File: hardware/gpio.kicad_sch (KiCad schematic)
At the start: 14 parts, among them U4 CCGM1A1

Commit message: Cleanup
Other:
- moved on the sheet: R115, R116, R117
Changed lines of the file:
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@@
 	(wire
 		(pts
-			(xy 234.95 35.56) (xy 234.95 38.1)
+			(xy 101.6 80.01) (xy 101.6 82.55)
 		)
 		(stroke
@@
 	(wire
 		(pts
-			(xy 229.87 35.56) (xy 229.87 38.1)
+			(xy 96.52 80.01) (xy 96.52 82.55)
 		)
 		(stroke
@@
 	(wire
 		(pts
-			(xy 234.95 25.4) (xy 234.95 30.48)
+			(xy 101.6 69.85) (xy 101.6 74.93)
 		)
 		(stroke
@@
 	(wire
 		(pts
-			(xy 224.79 30.48) (xy 224.79 25.4)
+			(xy 91.44 74.93) (xy 91.44 69.85)
 		)
 		(stroke
@@
 	(wire
 		(pts
-			(xy 224.79 35.56) (xy 224.79 38.1)
+			(xy 91.44 80.01) (xy 91.44 82.55)
 		)
 		(stroke
@@
 	(wire
 		(pts
-			(xy 229.87 25.4) (xy 229.87 30.48)
+			(xy 96.52 69.85) (xy 96.52 74.93)
 		)
 		(stroke
@@
 	(global_label "VDD_CLK"
 		(shape passive)
-		(at 229.87 25.4 90)
+		(at 96.52 69.85 90)
 		(fields_autoplaced yes)
 		(effects
@@
 		)
 		(property "Intersheetrefs" "${INTERSHEET_REFS}"
-			(at 229.87 15.3618 90)
+			(at 96.52 59.8118 90)
 			(effects
 				(font
@@
 	(symbol
 		(lib_id "Device:R_Small")
-		(at 229.87 33.02 180)
+		(at 96.52 77.47 180)
 		(unit 1)
 		(exclude_from_sim no)
@@
 		(dnp no)
 		(property "Reference" "R117"
-			(at 227.33 33.02 90)
+			(at 93.98 77.47 90)
 			(effects
 				(font
@@
 		)
 		(property "Value" "dnp"
-			(at 229.87 33.02 90)
+			(at 96.52 77.47 90)
 			(effects
 				(font
@@
 		)
 		(property "Footprint" "Resistor_SMD:R_0402_1005Metric"
-			(at 229.87 33.02 0)
+			(at 96.52 77.47 0)
 			(effects
 				(font
@@
 		)
 		(property "Datasheet" "~"
-			(at 229.87 33.02 0)
+			(at 96.52 77.47 0)
 			(effects
 				(font
@@
 		)
 		(property "Description" "Resistor, small symbol"
-			(at 229.87 33.02 0)
+			(at 96.52 77.47 0)
 			(effects
 				(font
@@
 	(symbol
 		(lib_id "power:VCC")
-		(at 229.87 38.1 180)
+		(at 96.52 82.55 180)
 		(unit 1)
 		(exclude_from_sim no)
@@
 		(dnp no)
 		(property "Reference" "#PWR0152"
-			(at 229.87 34.29 0)
+			(at 96.52 78.74 0)
 			(effects
 				(font
@@
 		)
 		(property "Value" "SDRAM_VCC"
-			(at 227.584 44.958 90)
+			(at 94.234 89.408 90)
 			(effects
 				(font
@@
 		)
 		(property "Footprint" ""
-			(at 229.87 38.1 0)
+			(at 96.52 82.55 0)
 			(effects
 				(font
@@
 		)
 		(property "Datasheet" ""
-			(at 229.87 38.1 0)
+			(at 96.52 82.55 0)
 			(effects
 				(font
@@
 		)
 		(property "Description" "Power symbol creates a global label with name \"VCC\""
-			(at 229.87 38.1 0)
+			(at 96.52 82.55 0)
 			(effects
 				(font
@@
 		(lib_name "+3V3_1")
 		(lib_id "power:+3V3")
-		(at 234.95 25.4 0)
+		(at 101.6 69.85 0)
 		(unit 1)
 		(exclude_from_sim no)
@@
 		(dnp no)
 		(property "Reference" "#PWR0135"
-			(at 234.95 29.21 0)
+			(at 101.6 73.66 0)
 			(effects
 				(font
@@
 		)
 		(property "Value" "+3V3"
-			(at 234.95 20.32 90)
+			(at 101.6 64.77 90)
 			(effects
 				(font
@@
 		)
 		(property "Footprint" ""
-			(at 234.95 25.4 0)
+			(at 101.6 69.85 0)
 			(effects
 				(font
@@
 		)
 		(property "Datasheet" ""
-			(at 234.95 25.4 0)
+			(at 101.6 69.85 0)
 			(effects
 				(font
@@
 		)
 		(property "Description" "Power symbol creates a global label with name \"+3V3\""
-			(at 234.95 25.4 0)
+			(at 101.6 69.85 0)
 			(effects
 				(font
@@
 	(symbol
 		(lib_id "Device:R_Small")
-		(at 234.95 33.02 180)
+		(at 101.6 77.47 180)
 		(unit 1)
 		(exclude_from_sim no)
@@
 		(dnp no)
 		(property "Reference" "R115"
-			(at 232.41 33.02 90)
+			(at 99.06 77.47 90)
 			(effects
 				(font
@@
 		)
 		(property "Value" "dnp"
-			(at 234.95 33.02 90)
+			(at 101.6 77.47 90)
 			(effects
 				(font
@@
 		)
 		(property "Footprint" "Resistor_SMD:R_0402_1005Metric"
-			(at 234.95 33.02 0)
+			(at 101.6 77.47 0)
 			(effects
 				(font
@@
 		)
 		(property "Datasheet" "~"
-			(at 234.95 33.02 0)
+			(at 101.6 77.47 0)
 			(effects
 				(font
@@
 		)
 		(property "Description" "Resistor, small symbol"
-			(at 234.95 33.02 0)
+			(at 101.6 77.47 0)
 			(effects
 				(font
@@
 	(symbol
 		(lib_id "power:+1V8")
-		(at 224.79 25.4 0)
+		(at 91.44 69.85 0)
 		(unit 1)
 		(exclude_from_sim no)
@@
 		(dnp no)
 		(property "Reference" "#PWR091"
-			(at 224.79 29.21 0)
+			(at 91.44 73.66 0)
 			(effects
 				(font
@@
 		)
 		(property "Value" "+1V8"
-			(at 224.79 20.32 90)
+			(at 91.44 64.77 90)
 			(effects
 				(font
@@
 		)
 		(property "Footprint" ""
-			(at 224.79 25.4 0)
+			(at 91.44 69.85 0)
 			(effects
 				(font
@@
 		)
 		(property "Datasheet" ""
-			(at 224.79 25.4 0)
+			(at 91.44 69.85 0)
 			(effects
 				(font
@@
 		)
 		(property "Description" "Power symbol creates a global label with name \"+1V8\""
-			(at 224.79 25.4 0)
+			(at 91.44 69.85 0)
 			(effects
 				(font
@@
 	(symbol
 		(lib_id "power:VCC")
-		(at 234.95 38.1 180)
+		(at 101.6 82.55 180)
 		(unit 1)
 		(exclude_from_sim no)
@@
 		(dnp no)
 		(property "Reference" "#PWR0151"
-			(at 234.95 34.29 0)
+			(at 101.6 78.74 0)
 			(effects
 				(font
@@
 		)
 		(property "Value" "SDRAM_VCC"
-			(at 232.664 44.958 90)
+			(at 99.314 89.408 90)
 			(effects
 				(font
@@
 		)
 		(property "Footprint" ""
-			(at 234.95 38.1 0)
+			(at 101.6 82.55 0)
 			(effects
 				(font
@@
 		)
 		(property "Datasheet" ""
-			(at 234.95 38.1 0)
+			(at 101.6 82.55 0)
 			(effects
 				(font
@@
 		)
 		(property "Description" "Power symbol creates a global label with name \"VCC\""
-			(at 234.95 38.1 0)
+			(at 101.6 82.55 0)
 			(effects
 				(font
@@
 	(symbol
 		(lib_id "power:VCC")
-		(at 224.79 38.1 180)
+		(at 91.44 82.55 180)
 		(unit 1)
 		(exclude_from_sim no)
@@
 		(dnp no)
 		(property "Reference" "#PWR0150"
-			(at 224.79 34.29 0)
+			(at 91.44 78.74 0)
 			(effects
 				(font
@@
 		)
 		(property "Value" "SDRAM_VCC"
-			(at 222.504 44.958 90)
+			(at 89.154 89.408 90)
 			(effects
 				(font
@@
 		)
 		(property "Footprint" ""
-			(at 224.79 38.1 0)
+			(at 91.44 82.55 0)
 			(effects
 				(font
@@
 		)
 		(property "Datasheet" ""
-			(at 224.79 38.1 0)
+			(at 91.44 82.55 0)
 			(effects
 				(font
@@
 		)
 		(property "Description" "Power symbol creates a global label with name \"VCC\""
-			(at 224.79 38.1 0)
+			(at 91.44 82.55 0)
 			(effects
 				(font
@@
 	(symbol
 		(lib_id "Device:R_Small")
-		(at 224.79 33.02 180)
+		(at 91.44 77.47 180)
 		(unit 1)
 		(exclude_from_sim no)
@@
 		(dnp no)
 		(property "Reference" "R116"
-			(at 223.012 32.766 90)
+			(at 89.662 77.216 90)
 			(effects
 				(font
@@
 		)
 		(property "Value" "0R"
-			(at 224.79 33.02 90)
+			(at 91.44 77.47 90)
 			(effects
 				(font
@@
 		)
 		(property "Footprint" "Resistor_SMD:R_0402_1005Metric"
-			(at 224.79 33.02 0)
+			(at 91.44 77.47 0)
 			(effects
 				(font
@@
 		)
 		(property "Datasheet" "~"
-			(at 224.79 33.02 0)
+			(at 91.44 77.47 0)
 			(effects
 				(font
@@
 		)
 		(property "Description" "Resistor, small symbol"
-			(at 224.79 33.02 0)
+			(at 91.44 77.47 0)
 			(effects
 				(font

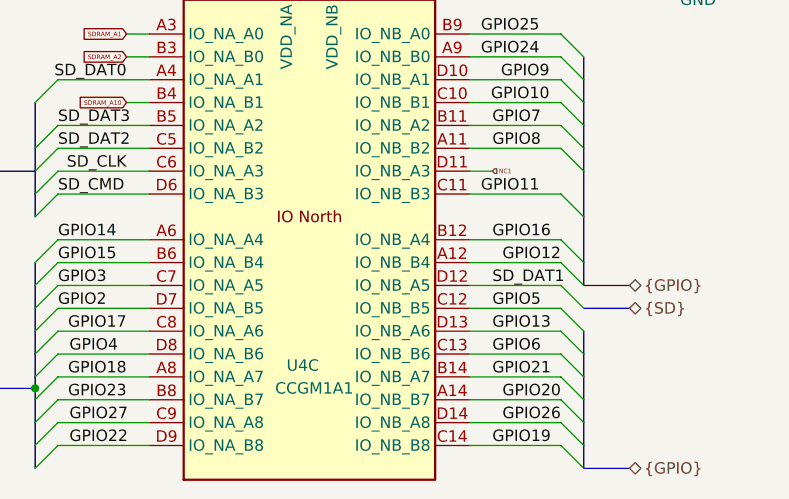
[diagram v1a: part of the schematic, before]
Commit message: Connecting PWR and FAN_PWM to NC pins, using NC3 for Ethernet clock
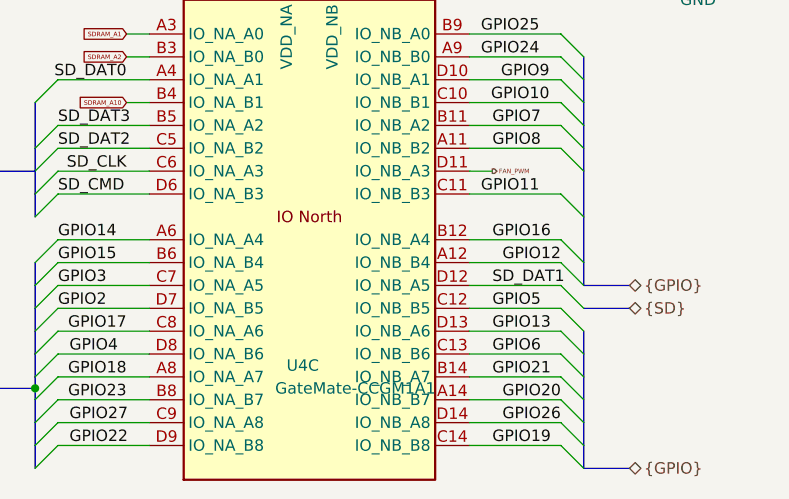
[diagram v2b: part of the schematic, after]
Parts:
- U4: value CCGM1A1 -> GateMate-CCGM1A1
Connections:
- net NC1 renamed FAN_PWM
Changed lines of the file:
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@@
 		)
 	)
-	(hierarchical_label "NC1"
-		(shape input)
+	(hierarchical_label "FAN_PWM"
+		(shape output)
 		(at 172.72 71.12 0)
 		(effects
@@
 			)
 		)
-		(property "Value" "CCGM1A1"
+		(property "Value" "GateMate-CCGM1A1"
 			(at 148.59 95.25 0)
 			(effects

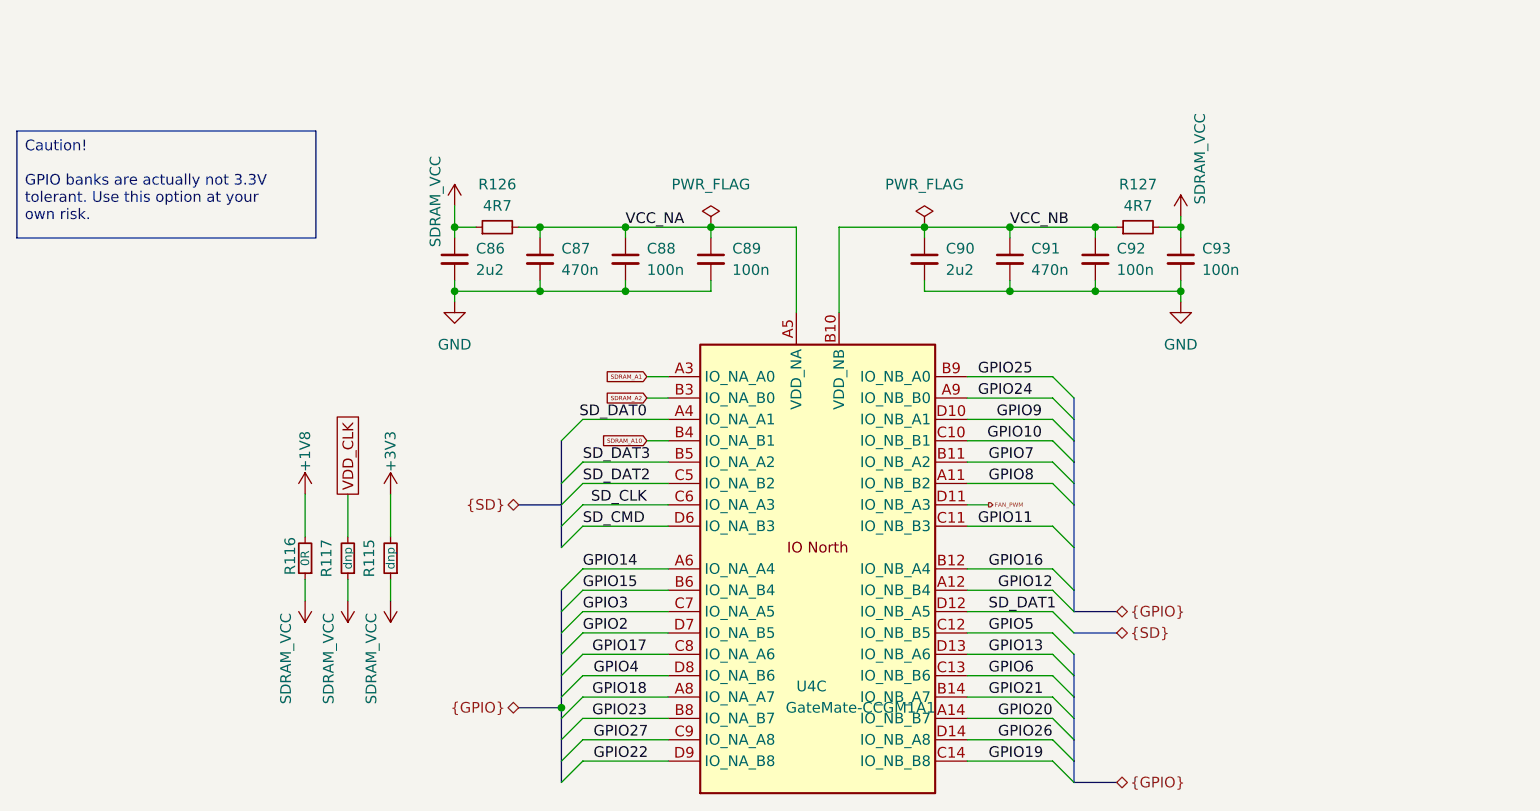
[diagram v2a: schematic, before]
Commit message: Updating sch - moving power select resistors to bottom
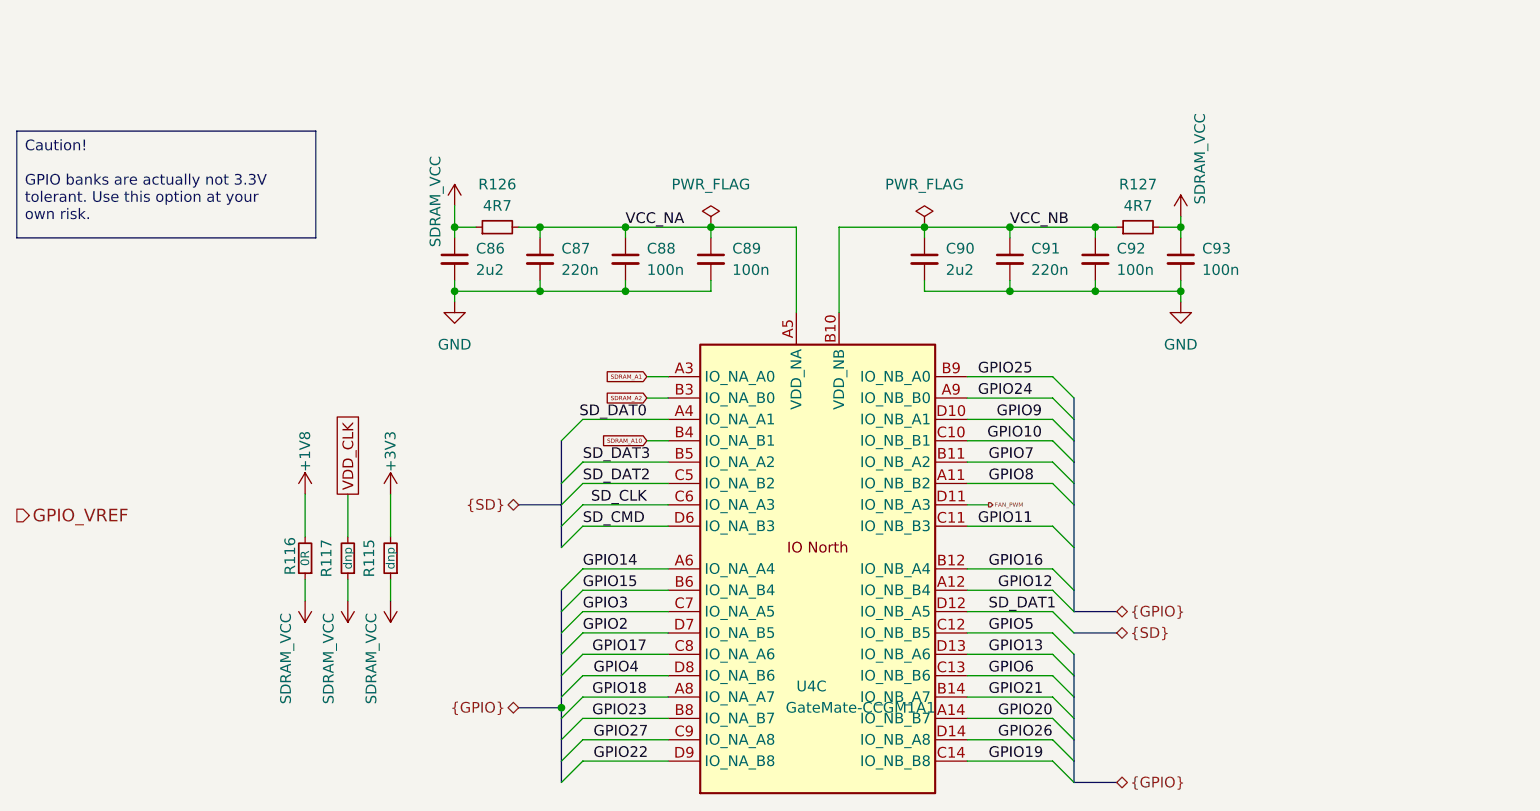
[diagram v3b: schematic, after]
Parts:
- C87, C91: value 470n -> 220n
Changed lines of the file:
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@@
+		)
+	)
+	(hierarchical_label "GPIO_VREF"
+		(shape output)
+		(at 57.15 72.39 0)
+		(effects
+			(font
+				(size 1.5 1.5)
+			)
+			(justify left)
 		)
 	)
@@
 		(fields_autoplaced yes)
 		(property "Reference" "C91"
-			(at 177.8 40.6463 0)
+			(at 177.8 40.6462 0)
 			(effects
 				(font
@@
 			)
 		)
-		(property "Value" "470n"
-			(at 177.8 43.1863 0)
+		(property "Value" "220n"
+			(at 177.8 43.1862 0)
 			(effects
 				(font
@@
 		(fields_autoplaced yes)
 		(property "Reference" "C87"
-			(at 121.92 40.6463 0)
+			(at 121.92 40.6462 0)
 			(effects
 				(font
@@
 			)
 		)
-		(property "Value" "470n"
-			(at 121.92 43.1863 0)
-			(effects
-				(font
+		(property "Value" "220n"
+			(at 121.92 43.1862 0)
+			(effects
+				(font

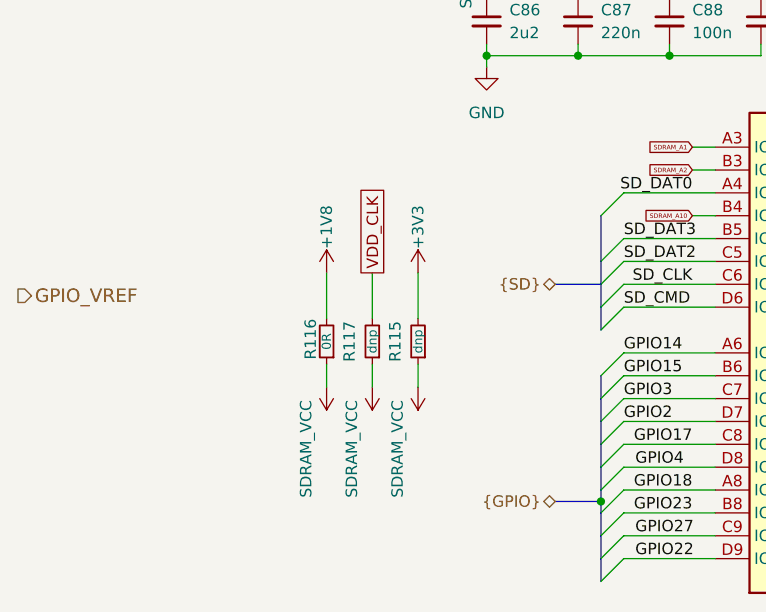
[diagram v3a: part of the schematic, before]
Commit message: Moving VDD_CLK to 1V8, removing 2V5 Fix #27
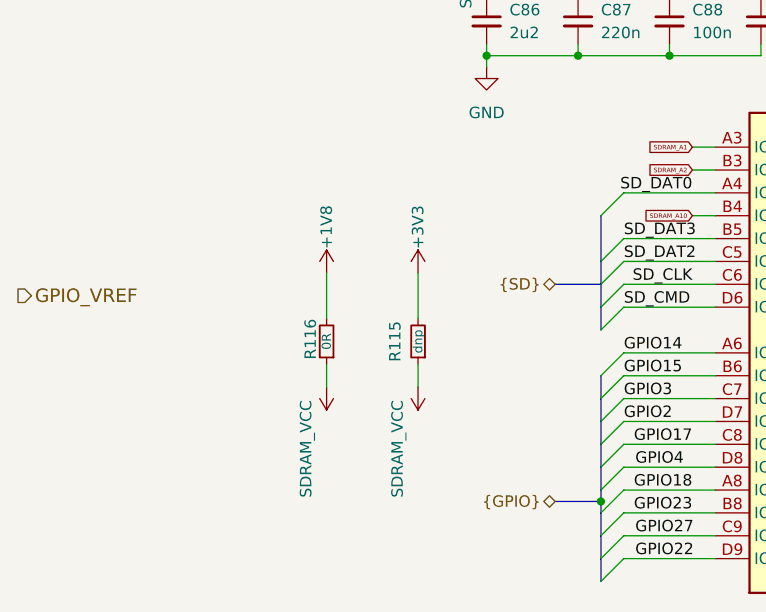
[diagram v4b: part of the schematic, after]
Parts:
- removed R117: dnp, Resistor_SMD:R_0402_1005Metric, symbol Device:R_Small
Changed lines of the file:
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@@
-	(wire
-		(pts
-			(xy 96.52 80.01) (xy 96.52 82.55)
-		)
-		(stroke
-			(width 0)
-			(type default)
-		)
-	)
 	(wire
 		(pts
@@
 		(pts
 			(xy 185.42 45.72) (xy 195.58 45.72)
-		)
-		(stroke
-			(width 0)
-			(type default)
-		)
-	)
-	(wire
-		(pts
-			(xy 96.52 69.85) (xy 96.52 74.93)
 		)
 		(stroke
@@
 				)
 				(justify right)
-				(hide yes)
-			)
-		)
-	)
-	(global_label "VDD_CLK"
-		(shape passive)
-		(at 96.52 69.85 90)
-		(fields_autoplaced yes)
-		(effects
-			(font
-				(size 1.27 1.27)
-			)
-			(justify left)
-		)
-		(property "Intersheetrefs" "${INTERSHEET_REFS}"
-			(at 96.52 59.8118 90)
-			(effects
-				(font
-					(size 1.27 1.27)
-				)
-				(justify left)
 				(hide yes)
 			)
@@
 					(unit 1)
 				)
-			)
-		)
-	)
-	(symbol
-		(lib_id "Device:R_Small")
-		(at 96.52 77.47 180)
-		(unit 1)
-		(exclude_from_sim no)
-		(in_bom yes)
-		(on_board yes)
-		(dnp no)
-		(property "Reference" "R117"
-			(at 93.98 77.47 90)
-			(effects
-				(font
-					(size 1.27 1.27)
-				)
-			)
-		)
-		(property "Value" "dnp"
-			(at 96.52 77.47 90)
-			(effects
-				(font
-					(size 1.016 1.016)
-				)
-			)
-		)
-		(property "Footprint" "Resistor_SMD:R_0402_1005Metric"
-			(at 96.52 77.47 0)
-			(effects
-				(font
-					(size 1.27 1.27)
-				)
-				(hide yes)
-			)
-		)
-		(property "Datasheet" "~"
-			(at 96.52 77.47 0)
-			(effects
-				(font
-					(size 1.27 1.27)
-				)
-				(hide yes)
-			)
-		)
-		(property "Description" "Resistor, small symbol"
-			(at 96.52 77.47 0)
-			(effects
-				(font
-					(size 1.27 1.27)
-				)
-				(hide yes)
-			)
-		)
-		(pin "1"
-		)
-		(pin "2"
-		)
-		(instances
-			(project "ulx5m-gs"
-				(path "/9e5cbfd6-8186-4817-919e-acd256336bc8/a29a432d-2cca-4e45-9947-735d9a1918bd"
-					(reference "R117")
-					(unit 1)
-				)
-			)
-		)
-	)
-	(symbol
-		(lib_id "power:VCC")
-		(at 96.52 82.55 180)
-		(unit 1)
-		(exclude_from_sim no)
-		(in_bom yes)
-		(on_board yes)
-		(dnp no)
-		(property "Reference" "#PWR0152"
-			(at 96.52 78.74 0)
-			(effects
-				(font
-					(size 1.27 1.27)
-				)
-				(hide yes)
-			)
-		)
-		(property "Value" "SDRAM_VCC"
-			(at 94.234 89.408 90)
-			(effects
-				(font
-					(size 1.27 1.27)
-				)
-			)
-		)
-		(property "Footprint" ""
-			(at 96.52 82.55 0)
-			(effects
-				(font
-					(size 1.27 1.27)
-				)
-				(hide yes)
-			)
-		)
-		(property "Datasheet" ""
-			(at 96.52 82.55 0)
-			(effects
-				(font
-					(size 1.27 1.27)
-				)
-				(hide yes)
-			)
-		)
-		(property "Description" "Power symbol creates a global label with name \"VCC\""
-			(at 96.52 82.55 0)
-			(effects
-				(font
-					(size 1.27 1.27)
-				)
-				(hide yes)
-			)
-		)
-		(pin "1"
-		)
-		(instances
-			(project "ulx5m-gs"
-				(path "/9e5cbfd6-8186-4817-919e-acd256336bc8/a29a432d-2cca-4e45-9947-735d9a1918bd"
-					(reference "#PWR0152")
-					(unit 1)
-				)

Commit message: CleanUP
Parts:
- removed R126, R127: 4R7, Resistor_SMD:R_0402_1005Metric, symbol Device:R_Small
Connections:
- net VCC_NA is gone; now on net SDRAM_VCC: C87.1, C88.1, C89.1, U4.A5 (VDD_NA), U4.B7 (VDD_NA), U4.E6 (VDD_NA), U4.E8 (VDD_NA), U4.F7 (VDD_NA)
- net VCC_NB is gone; now on net SDRAM_VCC: C90.1, C91.1, C92.1, U4.B10 (VDD_NB), U4.B13 (VDD_NB), U4.E10 (VDD_NB), U4.E12 (VDD_NB), U4.F11 (VDD_NB)
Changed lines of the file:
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@@
 	(wire
 		(pts
-			(xy 109.22 38.1) (xy 111.76 38.1)
+			(xy 109.22 38.1) (xy 119.38 38.1)
 		)
 		(stroke
@@
 	(wire
 		(pts
-			(xy 185.42 38.1) (xy 187.96 38.1)
+			(xy 185.42 38.1) (xy 195.58 38.1)
 		)
 		(stroke
@@
 	(wire
 		(pts
-			(xy 193.04 38.1) (xy 195.58 38.1)
-		)
-		(stroke
-			(width 0)
-			(type default)
-		)
-	)
-	(wire
-		(pts
 			(xy 195.58 38.1) (xy 195.58 39.37)
 		)
@@
 		(pts
 			(xy 121.92 73.66) (xy 121.92 76.2)
-		)
-		(stroke
-			(width 0)
-			(type default)
-		)
-	)
-	(wire
-		(pts
-			(xy 116.84 38.1) (xy 119.38 38.1)
 		)
 		(stroke
@@
 			)
 			(justify left)
-		)
-	)
-	(symbol
-		(lib_id "Device:R_Small")
-		(at 190.5 38.1 90)
-		(unit 1)
-		(exclude_from_sim no)
-		(in_bom yes)
-		(on_board yes)
-		(dnp no)
-		(property "Reference" "R127"
-			(at 190.5 33.02 90)
-			(effects
-				(font
-					(size 1.27 1.27)
-				)
-			)
-		)
-		(property "Value" "4R7"
-			(at 190.5 35.56 90)
-			(effects
-				(font
-					(size 1.27 1.27)
-				)
-			)
-		)
-		(property "Footprint" "Resistor_SMD:R_0402_1005Metric"
-			(at 190.5 38.1 0)
-			(effects
-				(font
-					(size 1.27 1.27)
-				)
-				(hide yes)
-			)
-		)
-		(property "Datasheet" "~"
-			(at 190.5 38.1 0)
-			(effects
-				(font
-					(size 1.27 1.27)
-				)
-				(hide yes)
-			)
-		)
-		(property "Description" "Resistor, small symbol"
-			(at 190.5 38.1 0)
-			(effects
-				(font
-					(size 1.27 1.27)
-				)
-				(hide yes)
-			)
-		)
-		(pin "1"
-		)
-		(pin "2"
-		)
-		(instances
-			(project "ulx5m-gs"
-				(path "/9e5cbfd6-8186-4817-919e-acd256336bc8/a29a432d-2cca-4e45-9947-735d9a1918bd"
-					(reference "R127")
-					(unit 1)
-				)
-			)
 		)
 	)
@@
 					(unit 1)
 				)
-			)
-		)
-	)
-	(symbol
-		(lib_id "Device:R_Small")
-		(at 114.3 38.1 90)
-		(unit 1)
-		(exclude_from_sim no)
-		(in_bom yes)
-		(on_board yes)
-		(dnp no)
-		(property "Reference" "R126"
-			(at 114.3 33.02 90)
-			(effects
-				(font
-					(size 1.27 1.27)
-				)
-			)
-		)
-		(property "Value" "4R7"
-			(at 114.3 35.56 90)
-			(effects
-				(font
-					(size 1.27 1.27)
-				)
-			)
-		)
-		(property "Footprint" "Resistor_SMD:R_0402_1005Metric"
-			(at 114.3 38.1 0)
-			(effects
-				(font
-					(size 1.27 1.27)
-				)
-				(hide yes)
-			)
-		)
-		(property "Datasheet" "~"
-			(at 114.3 38.1 0)
-			(effects
-				(font
-					(size 1.27 1.27)
-				)
-				(hide yes)
-			)
-		)
-		(property "Description" "Resistor, small symbol"
-			(at 114.3 38.1 0)
-			(effects
-				(font
-					(size 1.27 1.27)
-				)
-				(hide yes)
-			)
-		)
-		(pin "1"
-		)
-		(pin "2"
-		)
-		(instances
-			(project "ulx5m-gs"
-				(path "/9e5cbfd6-8186-4817-919e-acd256336bc8/a29a432d-2cca-4e45-9947-735d9a1918bd"
-					(reference "R126")
-					(unit 1)
-				)
